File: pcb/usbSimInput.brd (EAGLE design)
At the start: 65.7 x 63.5 mm, 24 parts, among them U1 MEGA16-P, X1 12MHz

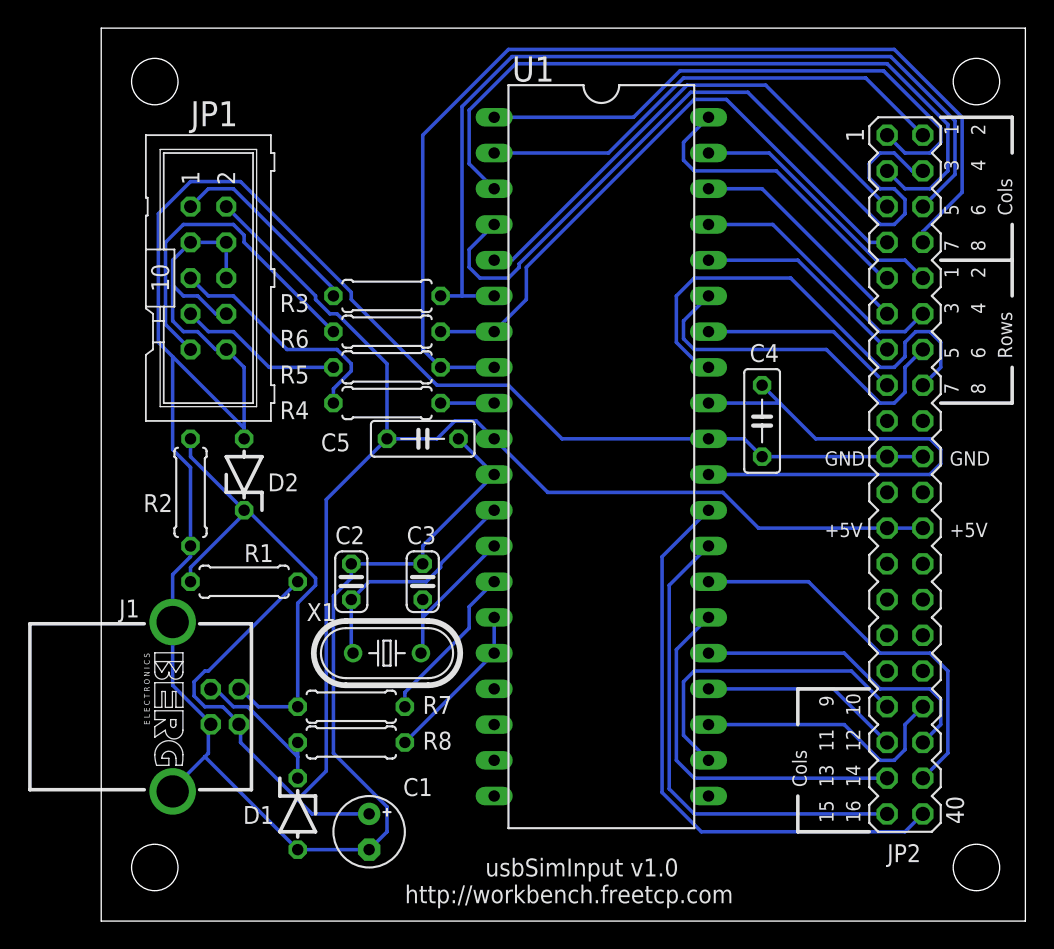
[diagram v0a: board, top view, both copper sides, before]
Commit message: connected unused PORTD pins to header made board smaller
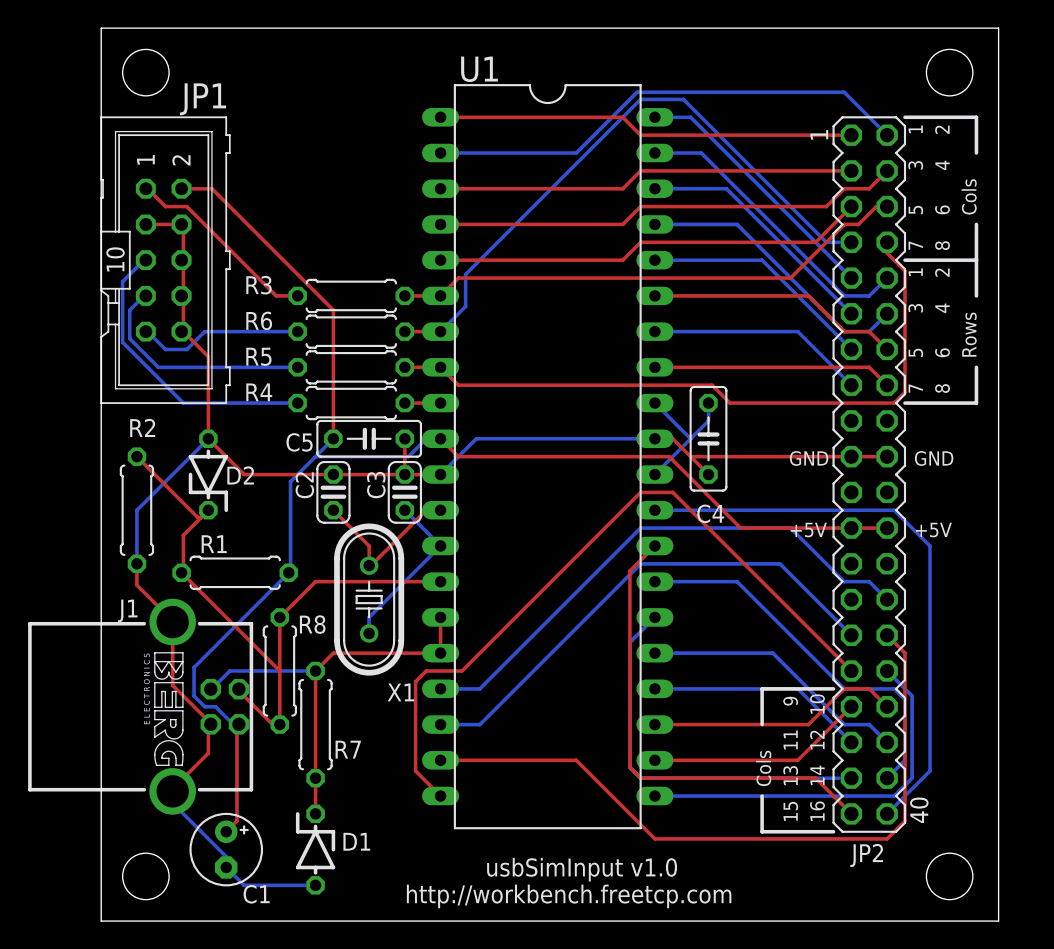
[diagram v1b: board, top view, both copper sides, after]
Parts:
- moved C1 10.2 mm to (8.89, 5.08)
- moved R8 7.18 mm to (12.7, 17.8), turned to 90 degrees
- moved C2 6.48 mm to (16.5, 30.5)
- moved C3 6.48 mm to (21.6, 30.5)
- moved C4 4.02 mm to (43.2, 34.3)
- moved R2 4.02 mm to (2.54, 29.2)
- moved X1 4.02 mm to (19.1, 22.9), turned to 270 degrees
- moved U1 3.81 mm to (31.8, 33.0)
- moved C5 3.81 mm to (19.1, 34.3)
- moved JP1 3.42 mm to (4.45, 47.0)
- moved R7 2.84 mm to (15.2, 14.0), turned to 90 degrees
- moved D1 2.84 mm to (15.2, 5.08)
- moved D2 2.54 mm to (7.62, 31.8)
- moved JP2 2.54 mm to (54.6, 31.8)
- moved R3 2.54 mm to (17.8, 44.5)
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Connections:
- removed net N$10: R8.1, U1.15, U1.16
- removed net N$9: R7.1, U1.14
- new net PD3: JP2.28, U1.17
- new net PD4: JP2.29, U1.18
- new net PD5: JP2.30, U1.19
- new net PD6: JP2.31, U1.20
- new net PD7: JP2.32, U1.21
- net USB+: now also R7.1, R7.2, U1.15, U1.16; no longer R8.2
- net USB-: now also R8.1, R8.2, U1.14; no longer R7.2
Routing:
- net GND: track 197.6 -> 118.7 mm
- net PD6: track 0.00 -> 50.7 mm
- net PD5: track 0.00 -> 49.6 mm
- net PD3: track 0.00 -> 38.6 mm
- net PD4: track 0.00 -> 36.0 mm
- net N$7: track 37.5 -> 10.3 mm
- net PD7: track 0.00 -> 27.2 mm
- net PB5: track 62.7 -> 36.9 mm
- net PB7: track 73.8 -> 48.1 mm
- net PB2: track 52.2 -> 29.7 mm
- net PB3: track 54.8 -> 33.3 mm
- net USB+: track 10.8 -> 30.1 mm
- net VCC: track 119.6 -> 101.8 mm
- net PA7: track 33.8 -> 17.0 mm
- net N$4: track 24.3 -> 11.8 mm
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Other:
- board size 65.7 x 63.5 mm -> 63.8 x 63.5 mm

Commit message: pcb rev to 1.01, fixed several errors and tweaked firmware enumerates
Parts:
- added R9: 10K, resistor:0207/7
- R2: value 4K7 -> 1M
- moved R2 30.0 mm to (20.3, 5.08), turned to 270 degrees
- moved R7 2.84 mm to (16.5, 11.4)
- moved R8 1.27 mm to (14.0, 17.8)
- moved D1 1.27 mm to (14.0, 5.08)
- moved R1 1.27 mm to (10.8, 24.8)
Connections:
- removed net PD3: JP2.28, U1.17
- new net N$9: D1.C, J1.3, R2.1, R7.1
- new net U-RST: R1.2, U1.17
- net GND: no longer JP1.3, R2.1
- net N$7: now also D2.C, J1.2, R1.1, R8.1; no longer C4.1, U1.30, U1.32
- net RESET: now also R9.2
- net USB+: no longer D1.C, J1.3, R7.1
- net USB-: no longer D2.C, J1.2, R1.1, R2.2, R8.1
- net VCC: now also C4.1, R2.2, R9.1, U1.30, U1.32; no longer R1.2
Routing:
- net PD3: track 38.6 -> 0.00 mm
- net USB-: track 45.6 -> 11.2 mm
- net VCC: track 101.8 -> 124.8 mm
- net N$9: track 0.00 -> 19.0 mm
- net USB+: track 30.1 -> 11.7 mm
- net U-RST: track 0.00 -> 13.8 mm
- net RESET: track 2.54 -> 16.3 mm
- net N$7: track 10.3 -> 19.5 mm
- net GND: track 118.7 -> 111.7 mm
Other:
- board text added: "usbSimInput v1.01"
- board text removed: "usbSimInput v1.0"

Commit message: fixed AREF->VCC error
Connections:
- new net N$8: C4.1, U1.32
- net VCC: no longer C4.1, U1.32
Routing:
- net VCC: track 124.8 -> 114.6 mm
- net N$8: track 0.00 -> 3.81 mm
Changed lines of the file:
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@@
 <wire x1="39.37" y1="33.02" x2="40.386" y2="33.02" width="0.254" layer="1"/>
 <wire x1="24.13" y1="34.29" x2="25.4" y2="33.02" width="0.254" layer="1"/>
-<contactref element="C4" pad="1"/>
-<contactref element="U1" pad="32"/>
-<contactref element="U1" pad="30"/>
-<wire x1="43.18" y1="35.56" x2="41.91" y2="34.29" width="0.254" layer="16"/>
-<wire x1="41.91" y1="34.29" x2="39.37" y2="31.75" width="0.254" layer="16"/>
-<wire x1="43.18" y1="36.83" x2="43.18" y2="35.56" width="0.254" layer="16"/>
-<wire x1="41.91" y1="34.29" x2="39.37" y2="36.83" width="0.254" layer="16"/>
 <contactref element="R9" pad="1"/>
 <wire x1="12.192" y1="47.752" x2="13.97" y2="49.53" width="0.254" layer="1"/>
-<wire x1="39.37" y1="31.75" x2="39.37" y2="33.02" width="0.254" layer="1"/>
 <wire x1="9.906" y1="14.986" x2="9.906" y2="14.224" width="0.254" layer="16"/>
 <wire x1="12.7" y1="17.78" x2="9.906" y2="14.986" width="0.254" layer="16"/>
@@
 <wire x1="16.764" y1="1.27" x2="20.32" y2="1.27" width="0.254" layer="1"/>
 <wire x1="9.652" y1="8.382" x2="16.764" y2="1.27" width="0.254" layer="1"/>
+<contactref element="U1" pad="30"/>
+<wire x1="39.37" y1="33.02" x2="39.37" y2="31.75" width="0.254" layer="1"/>
 </signal>
 <signal name="USB-">
@@
 <wire x1="14.732" y1="24.638" x2="14.605" y2="24.765" width="0.254" layer="16"/>
 </signal>
+<signal name="N$8">
+<contactref element="C4" pad="1"/>
+<contactref element="U1" pad="32"/>
+<wire x1="43.18" y1="36.83" x2="39.37" y2="36.83" width="0.254" layer="1"/>
+</signal>
 </signals>

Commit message: edited USB connector silkscreen
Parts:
- J1: value (none) -> PN61729-S
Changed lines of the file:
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@@
 <?xml version="1.0" encoding="utf-8"?>
 <!DOCTYPE eagle SYSTEM "eagle.dtd">
-<eagle version="6.1">
+<eagle version="7.2.0">
 <drawing>
 <settings>
@@
 </class>
 </classes>
-<designrules>
+<designrules name="SeeedStudio_2layer_DRU_no_angle_20140221">
 <description language="de">&lt;b&gt;EAGLE Design Rules&lt;/b&gt;
 &lt;p&gt;
@@
 </description>
 <param name="layerSetup" value="(1*16)"/>
-<param name="mtCopper" value="0.035mm 0.035mm 0.035mm 0.035mm 0.035mm 0.035mm 0.035mm 0.035mm 0.035mm 0.035mm 0.035mm 0.035mm 0.035mm 0.035mm 0.035mm 0.035mm"/>
-<param name="mtIsolate" value="1.5mm 0.15mm 0.2mm 0.15mm 0.2mm 0.15mm 0.2mm 0.15mm 0.2mm 0.15mm 0.2mm 0.15mm 0.2mm 0.15mm 0.2mm"/>
-<param name="mdWireWire" value="10mil"/>
-<param name="mdWirePad" value="10mil"/>
-<param name="mdWireVia" value="10mil"/>
-<param name="mdPadPad" value="10mil"/>
-<param name="mdPadVia" value="10mil"/>
-<param name="mdViaVia" value="10mil"/>
+<param name="mtCopper" value="0.035mm 0.0175mm 0.035mm 0.035mm 0.035mm 0.035mm 0.035mm 0.035mm 0.035mm 0.035mm 0.035mm 0.035mm 0.035mm 0.035mm 0.0175mm 0.035mm"/>
+<param name="mtIsolate" value="1.5mm 1.1mm 0.2mm 0.15mm 0.2mm 0.15mm 0.2mm 0.15mm 0.2mm 0.15mm 0.2mm 0.15mm 0.2mm 0.15mm 0.2mm"/>
+<param name="mdWireWire" value="6mil"/>
+<param name="mdWirePad" value="6mil"/>
+<param name="mdWireVia" value="6mil"/>
+<param name="mdPadPad" value="6mil"/>
+<param name="mdPadVia" value="6mil"/>
+<param name="mdViaVia" value="6mil"/>
 <param name="mdSmdPad" value="0mil"/>
 <param name="mdSmdVia" value="0mil"/>
@@
 <param name="mdDrill" value="10mil"/>
 <param name="mdSmdStop" value="0mil"/>
-<param name="msWidth" value="10mil"/>
+<param name="msWidth" value="6mil"/>
 <param name="msDrill" value="12mil"/>
 <param name="msMicroVia" value="12mil"/>
@@
 <pass name="Default">
 <param name="RoutingGrid" value="10mil"/>
+<param name="AutoGrid" value="1"/>
+<param name="Efforts" value="0"/>
+<param name="TopRouterVariant" value="1"/>
 <param name="tpViaShape" value="round"/>
 <param name="PrefDir.1" value="*"/>
@@
 <attribute name="VALUE" x="9.525" y="46.99" size="1.778" layer="27" ratio="10" rot="R270"/>
 </element>
-<element name="J1" library="con-berg" package="PN61729-S" value="" x="5.08" y="15.24" smashed="yes" rot="R270">
+<element name="J1" library="con-berg" package="PN61729-S" value="PN61729-S" x="5.08" y="15.24" smashed="yes" rot="R270">
 <attribute name="OC_NEWARK" value="unknown" x="-25.4" y="-6.35" size="1.778" layer="27" rot="R270" display="off"/>
 <attribute name="MPN" value="" x="-25.4" y="-6.35" size="1.778" layer="27" rot="R270" display="off"/>
@@
 </signal>
 </signals>
+<errors>
+</errors>
 </board>
 </drawing>
